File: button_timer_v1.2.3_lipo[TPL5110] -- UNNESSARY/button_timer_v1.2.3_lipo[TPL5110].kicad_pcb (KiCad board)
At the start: 2 copper layers, 21 x 41.7 mm, 25 parts, among them J1 Conn_01x05_Female, Q1 TSM2301ACX, Q2 TSM2301ACX, SW1 SW_Push, SW2 SW_Push, U1 TPL5110, U2 AP2112K-3.3, X1 ESP-12E

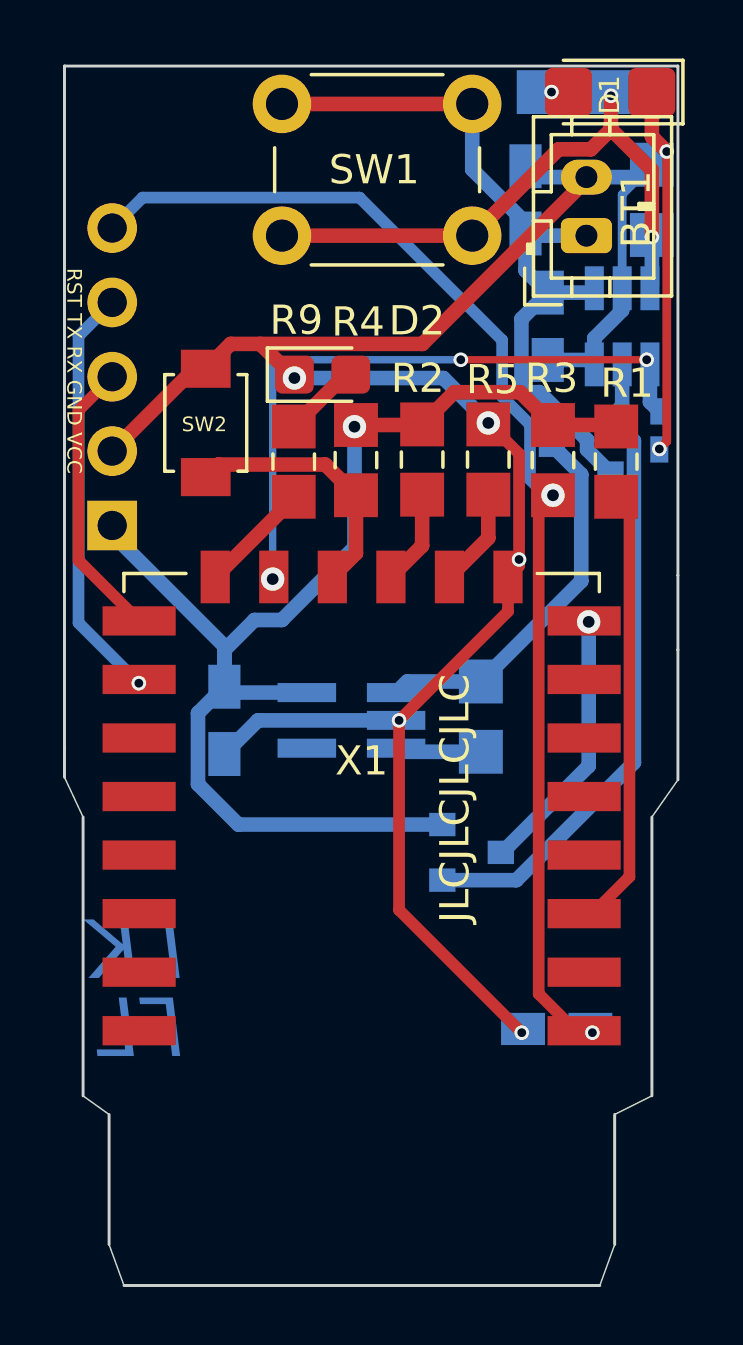
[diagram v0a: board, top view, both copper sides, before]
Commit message: cap between esp vcc and ground added
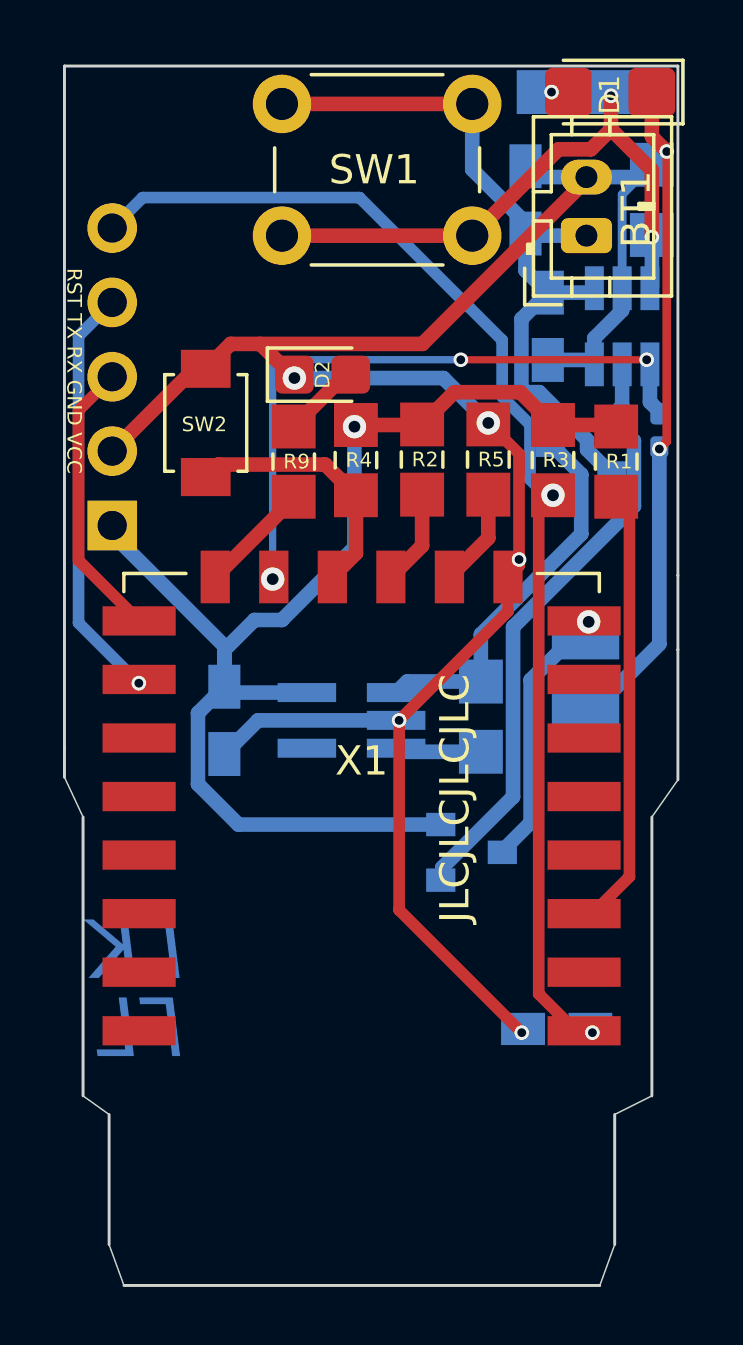
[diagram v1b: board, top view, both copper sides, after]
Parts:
- added C6: TAJB476M010TNJ, SamacSys_Parts:CAPPM3528X210N, B.Cu at (133.4, 81.5)
- D2: footprint LED_SMD:LED_0805_2012Metric_Castellated -> handsolder:LED_0805_2012Metric_Castellated_mod
- Q1, Q2: footprint Package_TO_SOT_SMD:SOT-23 -> handsolder:SOT-23
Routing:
- net /GND: track 86.5 -> 96.7 mm
- net Net-(Q1-Pad1): track 22.3 -> 20.8 mm
